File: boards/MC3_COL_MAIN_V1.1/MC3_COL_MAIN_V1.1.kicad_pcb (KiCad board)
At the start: 4 copper layers, 66 x 66 mm, 157 parts, among them J1 SUPPLY_IN, J10 MOTOR, J12 CAN, J13 HARNESS_FFC_6P, J2 SWD, J3 ENC_leaf1, J4 ENC_leaf2, J5 ENC_leaf3, J6 ENC_leaf4, J7 MOTOR, J8 MOTOR, J9 MOTOR, Q1 AO4421, SW1 SKRKAEE020, U1 AMS1117-3.3, U10 GP1S094HCZ0F, U11 GP1S094HCZ0F, U12 LM61460AANRJRR, U2 STM32U595RJT6, U3 DRV8214RTER, U4 DRV8214RTER, U5 DRV8214RTER, U6 DRV8214RTER, U7 DRV8214RTER, U8 TJA1051T/3, U9 AEDR-8300-1Q0, Y1 8MHz

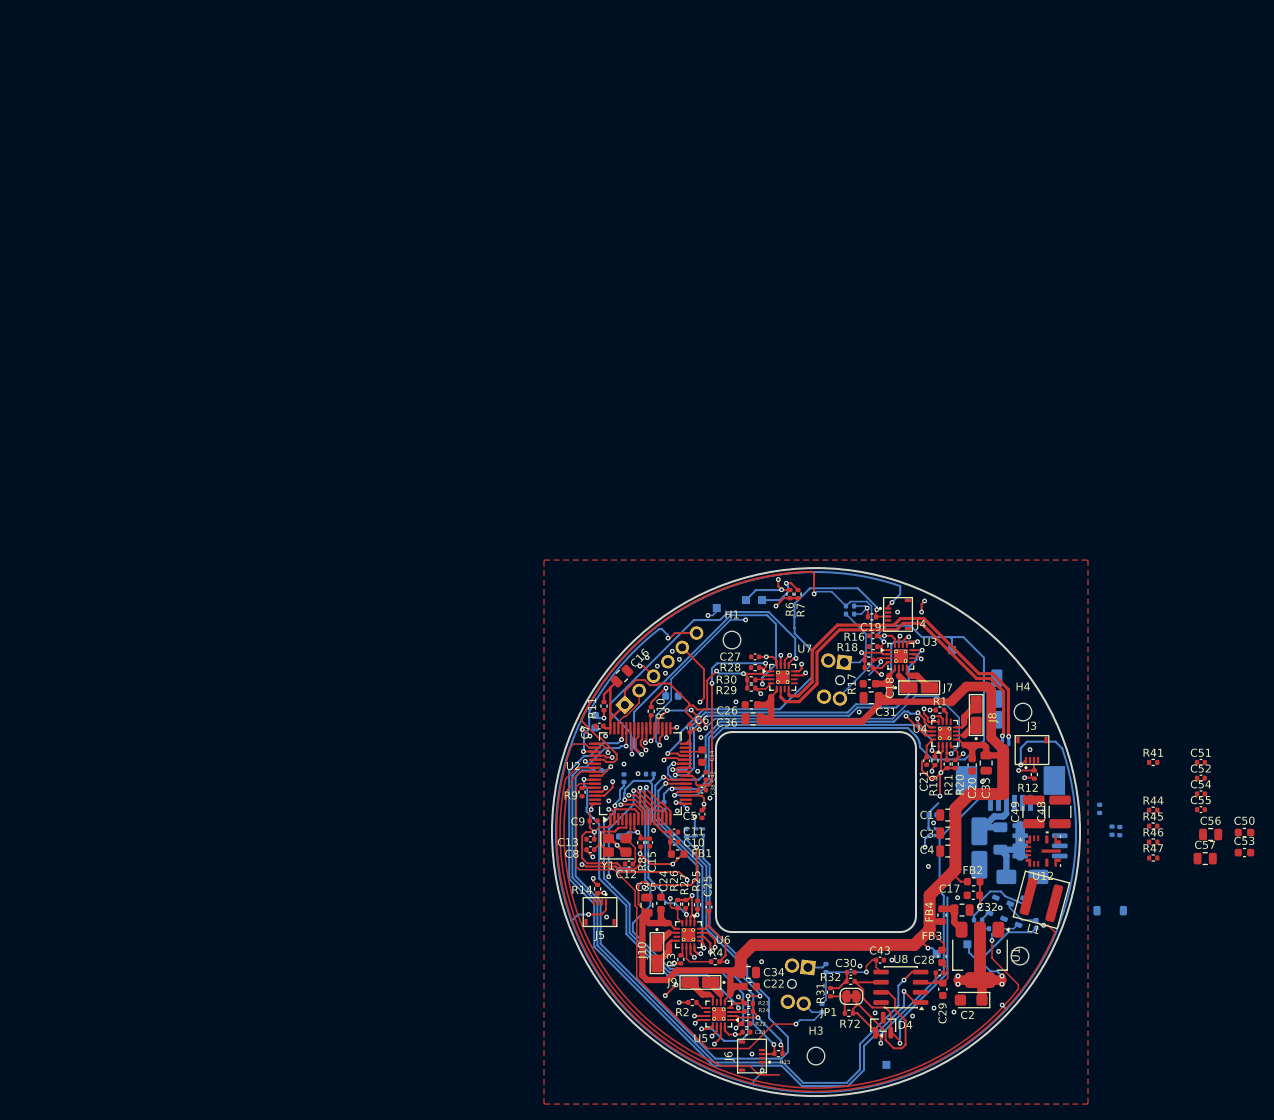
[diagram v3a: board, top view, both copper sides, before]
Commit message: V1.1: encoder FFC pin 4 -> RC_OUT_leafN (optical-fallback B channel over the open-drain ripple net); ERC 0 errors
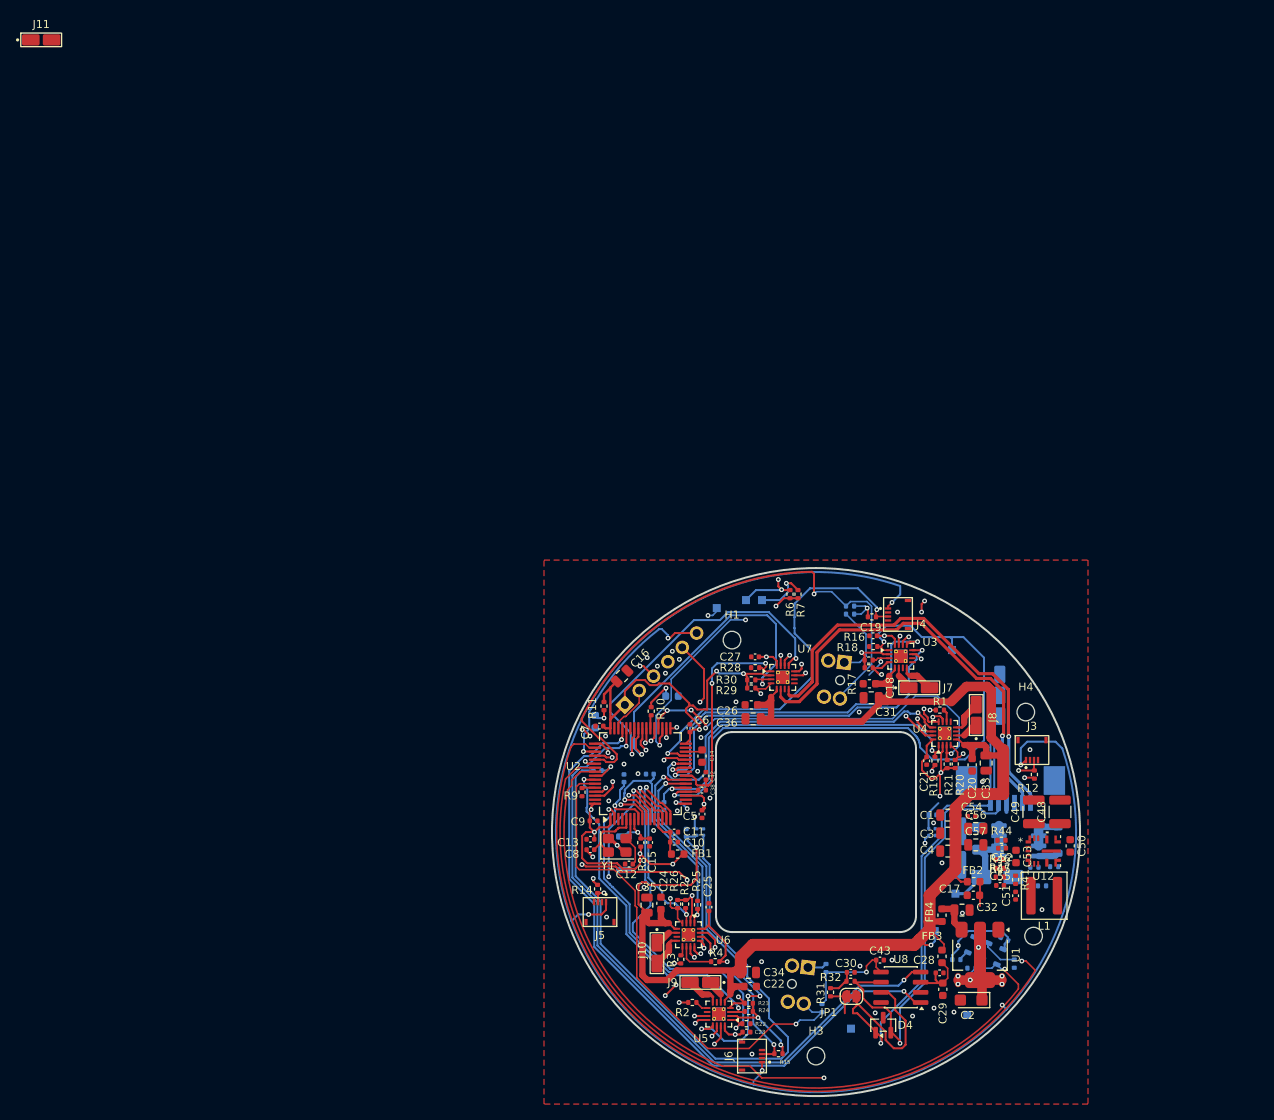
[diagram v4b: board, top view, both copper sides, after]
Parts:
- removed R72: 0R, MC3_COL_MAIN:R_0402_1005Metric
- added J11: MOTOR, MC3_COL_MAIN:SolderPads_2x_2.2x1.4mm_P2.6mm, F.Cu at (3.15, 0.97)
- moved C56 29.4 mm to (120.0, 99.5)
- moved C54 28.8 mm to (119.4, 98.0)
- moved C57 28.7 mm to (120.0, 101.6)
- moved C53 28.6 mm to (125.0, 103.0), turned to -90 degrees
- moved C51 28.5 mm to (125.0, 108.0), turned to 90 degrees
- moved C55 26.8 mm to (123.0, 106.7)
- moved C52 26.4 mm to (123.3, 102.0), turned to 180 degrees
- moved R41 22.6 mm to (125.0, 106.0), turned to -90 degrees
- moved C50 21.8 mm to (131.8, 101.7), turned to -90 degrees
- moved R45 19.6 mm to (123.0, 103.5), turned to 180 degrees
- moved R46 19.4 mm to (123.0, 104.5)
- moved R44 19.3 mm to (123.2, 101.0)
- moved R47 19.3 mm to (123.0, 105.6)
- moved R42 11.9 mm to (128.2, 106.7), turned to 0 degrees
- moved D7 11.0 mm to (130.2, 101.0), turned to -90 degrees
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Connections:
- net /Power/BUCK_RBOOT renamed Net-(U12-RBOOT)
- C51 pad 1: BUCK_SYNC -> /Power/BUCK_EN
- C51 pad 2: /Power/BUCK_EN -> BUCK_SYNC
- C55 pad 2: /Power/BUCK_FF -> Net-(C55-Pad2)
- J12 pad 1: CANH -> CANL
- J12 pad 2: CANL -> CANH
- J13 pad 1: YAW_OUT1 -> CANH
- J13 pad 2: YAW_OUT2 -> CANL
- J13 pad 5: CANH -> YAW_OUT1
- J13 pad 6: CANL -> YAW_OUT2
- R47 pad 1: /Power/BUCK_FF -> /Power/BUCK_FB
- R47 pad 2: /Power/BUCK_FB -> Net-(C55-Pad2)
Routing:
- net CANH: track 38.1 -> 79.1 mm, vias 0 -> 1
- net BUCK_SYNC: track 12.2 -> 51.6 mm, vias 0 -> 1
- net CANL: track 35.9 -> 66.7 mm
- net /CAN/CANH: track 26.5 -> 0.00 mm, vias 1 -> 0
- net +3V3: track 228.3 -> 208.4 mm
- net YAW_OUT1: track 45.4 -> 54.7 mm
- net YAW_OUT2: track 45.2 -> 53.6 mm
- net CAN1_RX: track 89.6 -> 84.2 mm
- net /Power/VIN_SW: track 0.00 -> 5.01 mm
- net CAN1_TX: track 89.3 -> 84.3 mm
- net VIN_PAD: track 8.45 -> 3.97 mm
- net VIN_PROT: track 10.2 -> 14.5 mm
- net /MCU/YAW_ENC_B: track 16.2 -> 13.2 mm, vias 1 -> 2
- net /Power/Q1_G: track 0.00 -> 2.54 mm
- net /MCU/YAW_ENC_A: track 10.9 -> 10.0 mm
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
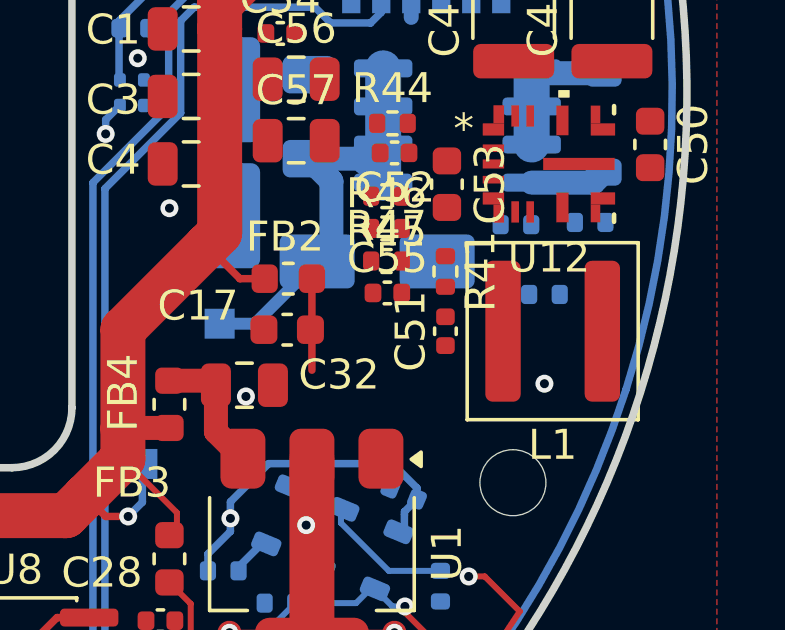
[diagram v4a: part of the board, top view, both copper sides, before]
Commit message: V1.1: encoder connector nets swapped to match placement (J3=leaf2, J4=leaf1, J5=leaf4, J6=leaf3)
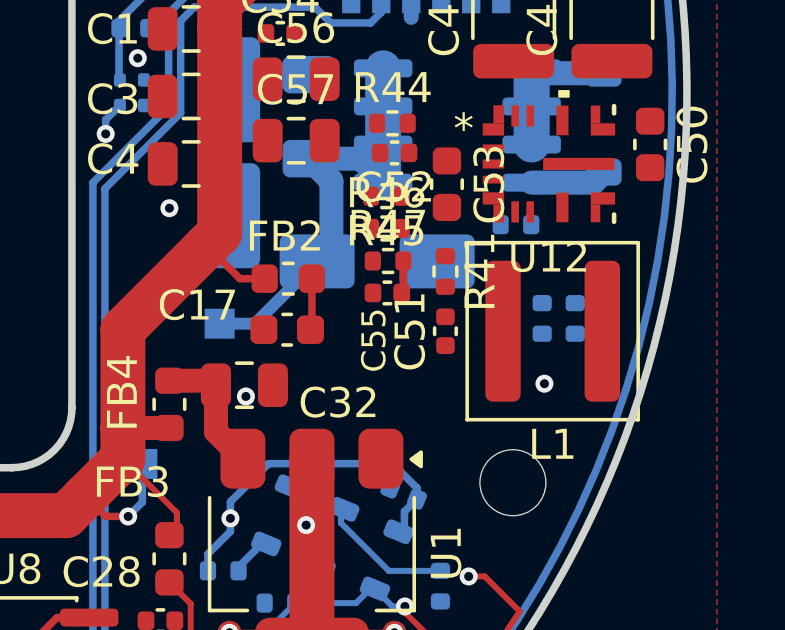
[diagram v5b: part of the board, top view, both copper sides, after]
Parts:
- moved R43 3.58 mm to (128.2, 107.5), turned to 90 degrees
- moved R42 1.30 mm to (129.3, 107.5), turned to -90 degrees
- moved R47 0.06 mm to (123.0, 105.6)
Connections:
- J3 pad 4: unconnected-(J3-Pin_4-Pad4) -> RC_OUT_leaf1
- J4 pad 4: unconnected-(J4-Pin_4-Pad4) -> RC_OUT_leaf2
- J5 pad 4: unconnected-(J5-Pin_4-Pad4) -> RC_OUT_leaf3
- J6 pad 4: unconnected-(J6-Pin_4-Pad4) -> RC_OUT_leaf4
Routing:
- net VSENS: track 51.1 -> 49.8 mm
- net Net-(C55-Pad2): track 0.00 -> 1.09 mm
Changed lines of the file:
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@@
 			(size 0.3 0.8)
 			(layers "F.Cu" "F.Mask" "F.Paste")
-			(net "unconnected-(J5-Pin_4-Pad4)")
+			(net "RC_OUT_leaf3")
 			(pinfunction "Pin_4_4")
-			(pintype "passive+no_connect")
+			(pintype "passive")
 		)
 		(pad "MP" smd rect
@@
 			(size 0.3 0.8)
 			(layers "F.Cu" "F.Mask" "F.Paste")
-			(net "unconnected-(J4-Pin_4-Pad4)")
+			(net "RC_OUT_leaf2")
 			(pinfunction "Pin_4_4")
-			(pintype "passive+no_connect")
+			(pintype "passive")
 		)
 		(pad "MP" smd rect
@@
 		(tags "capacitor")
 		(property "Reference" "C32"
-			(at 3.15 -0.35 0)
+			(at 3.15 0.6 0)
 			(layer "F.SilkS")
 			(effects
@@
 			(size 0.3 0.8)
 			(layers "F.Cu" "F.Mask" "F.Paste")
-			(net "unconnected-(J6-Pin_4-Pad4)")
+			(net "RC_OUT_leaf4")
 			(pinfunction "Pin_4_4")
-			(pintype "passive+no_connect")
+			(pintype "passive")
 		)
 		(pad "MP" smd rect
@@
 			(size 0.3 0.8)
 			(layers "F.Cu" "F.Mask" "F.Paste")
-			(net "unconnected-(J3-Pin_4-Pad4)")
+			(net "RC_OUT_leaf1")
 			(pinfunction "Pin_4_4")
-			(pintype "passive+no_connect")
+			(pintype "passive")
 		)
 		(pad "MP" smd rect
@@
 		(tags "capacitor")
 		(property "Reference" "C55"
-			(at 0 -1.16 0)
+			(at -0.44 1.575 90)
 			(layer "F.SilkS")
 			(effects
 				(font
-					(size 1 1)
+					(size 0.8 0.8)
 					(thickness 0.15)
 				)
@@
 	(footprint "MC3_COL_MAIN:R_0402_1005Metric"
 		(layer "F.Cu")
-		(at 122.985 105.61)
+		(at 123.04 105.61)
 		(descr "Resistor SMD 0402 (1005 Metric), square (rectangular) end terminal, IPC-7351 nominal, (Body size source: IPC-SM-782 page 72, https://www.pcb-3d.com/wordpress/wp-content/uploads/ipc-sm-782a_amendment_1_and_2.pdf)")
 		(tags "resistor")
@@
 		(tags "resistor")
 		(property "Reference" "R5"
-			(at 0.01 -1.25 0)
+			(at -0.025 -1.25 0)
 			(layer "B.SilkS")
 			(effects
@@
 	(footprint "MC3_COL_MAIN:R_0402_1005Metric"
 		(layer "B.Cu")
-		(at 128.25 106.725)
+		(at 129.275 107.525 -90)
 		(descr "Resistor SMD 0402 (1005 Metric), square (rectangular) end terminal, IPC-7351 nominal, (Body size source: IPC-SM-782 page 72, https://www.pcb-3d.com/wordpress/wp-content/uploads/ipc-sm-782a_amendment_1_and_2.pdf)")
 		(tags "resistor")
 		(property "Reference" "R42"
-			(at -2.716442 6.108824 0)
+			(at 0 -1.225 90)
 			(layer "B.SilkS")
 			(effects
@@
 		)
 		(property "Value" "100k"
-			(at 0 -1.17 0)
+			(at 0 -1.17 90)
 			(layer "B.Fab")
 			(effects
@@
 		)
 		(property "Datasheet" ""
-			(at 0 0 0)
+			(at 0 0 90)
 			(layer "B.Fab")
 			(hide yes)
@@
 		)
 		(property "Description" ""
-			(at 0 0 0)
+			(at 0 0 90)
 			(layer "B.Fab")
 			(hide yes)
@@
 		)
 		(property "KiLib_Generator" "SMD_2terminal_chip_molded"
-			(at 0 0 0)
+			(at 0 0 90)
 			(layer "B.SilkS")
 			(hide yes)
@@
 		(duplicate_pad_numbers_are_jumpers no)
 		(fp_line
-			(start -0.153641 -0.38)
-			(end 0.153641 -0.38)
+			(start -0.153641 0.38)
+			(end 0.153641 0.38)
 			(stroke
 				(width 0.12)
@@
 		)
 		(fp_line
-			(start -0.153641 0.38)
-			(end 0.153641 0.38)
+			(start -0.153641 -0.38)
+			(end 0.153641 -0.38)
 			(stroke
 				(width 0.12)
@@
 		)
 		(fp_text user "${REFERENCE}"
-			(at 0 0 0)
+			(at 0 0 90)
 			(layer "B.Fab")
 			(effects
@@
 		)
 		(pad "1" smd roundrect
-			(at -0.51 0)
+			(at -0.51 0 270)
 			(size 0.54 0.64)
 			(layers "B.Cu" "B.Mask" "B.Paste")
@@
 		)
 		(pad "2" smd roundrect
-			(at 0.51 0)
+			(at 0.51 0 270)
 			(size 0.54 0.64)
 			(layers "B.Cu" "B.Mask" "B.Paste")
@@
 	(footprint "MC3_COL_MAIN:R_0402_1005Metric"
 		(layer "B.Cu")
-		(at 129.775 104.325)
+		(at 128.175 107.525 90)
 		(descr "Resistor SMD 0402 (1005 Metric), square (rectangular) end terminal, IPC-7351 nominal, (Body size source: IPC-SM-782 page 72, https://www.pcb-3d.com/wordpress/wp-content/uploads/ipc-sm-782a_amendment_1_and_2.pdf)")
 		(tags "resistor")
 		(property "Reference" "R43"
-			(at 0 1.17 0)
+			(at 0 -1.25 90)
 			(layer "B.SilkS")
 			(effects
@@
 		)
 		(property "Value" "8.66k"
-			(at 0 -1.17 0)
+			(at 0 -1.17 90)
 			(layer "B.Fab")
 			(effects
@@
 		)
 		(property "Datasheet" ""
-			(at 0 0 0)
+			(at 0 0 90)
 			(layer "B.Fab")
 			(hide yes)
@@
 		)
 		(property "Description" ""
-			(at 0 0 0)
+			(at 0 0 90)
 			(layer "B.Fab")
 			(hide yes)
@@
 		)
 		(property "KiLib_Generator" "SMD_2terminal_chip_molded"
-			(at 0 0 0)
+			(at 0 0 90)
 			(layer "B.SilkS")
 			(hide yes)
@@
 		)
 		(fp_text user "${REFERENCE}"
-			(at 0 0 0)
+			(at 0 0 90)
 			(layer "B.Fab")
 			(effects
@@
 		)
 		(pad "1" smd roundrect
-			(at -0.51 0)
+			(at -0.51 0 90)
 			(size 0.54 0.64)
 			(layers "B.Cu" "B.Mask" "B.Paste")
@@
 		)
 		(pad "2" smd roundrect
-			(at 0.51 0)
+			(at 0.51 0 90)
 			(size 0.54 0.64)
 			(layers "B.Cu" "B.Mask" "B.Paste")
@@
 	)
 	(segment
-		(start 120.5 109.25)
-		(end 120.5 107.95)
-		(width 0.25)
-		(layer "F.Cu")
-		(net "VSENS")
-	)
-	(segment
 		(start 125.6 91.6)
 		(end 125.65 91.6)
@@
 	)
 	(segment
-		(start 103.6 120.71)
-		(end 103.6 122.65)
-		(width 0.25)
-		(layer "F.Cu")
-		(net "/CAN/TERM_H")
-	)
-	(segment
-		(start 101.815 120.535)
-		(end 103.775 120.535)
-		(width 0.25)
-		(layer "F.Cu")
-		(net "/CAN/TERM_H")
-	)
-	(segment
-		(start 103.775 120.535)
-		(end 103.6 120.71)
-		(width 0.25)
-		(layer "F.Cu")
-		(net "/CAN/TERM_H")
-	)
-	(segment
 		(start 91.778022 129.278022)
 		(end 88.379002 129.278022)
@@
 	)
 	(segment
+		(start 103.6 120.71)
+		(end 103.6 122.65)
+		(width 0.25)
+		(layer "F.Cu")
+		(net "/CAN/TERM_H")
+	)
+	(segment
+		(start 101.815 120.535)
+		(end 103.775 120.535)
+		(width 0.25)
+		(layer "F.Cu")
+		(net "/CAN/TERM_H")
+	)
+	(segment
+		(start 103.775 120.535)
+		(end 103.6 120.71)
+		(width 0.25)
+		(layer "F.Cu")
+		(net "/CAN/TERM_H")
+	)
+	(segment
 		(start 103.68 118.785)
 		(end 103.57 118.785)
@@
 	)
 	(segment
+		(start 123.55 105.61)
+		(end 123.55 106.62)
+		(width 0.25)
+		(layer "F.Cu")
+		(net "Net-(C55-Pad2)")
+	)
+	(segment
+		(start 123.55 106.62)
+		(end 123.495 106.675)
+		(width 0.25)
+		(layer "F.Cu")
+		(net "Net-(C55-Pad2)")
+	)
+	(segment

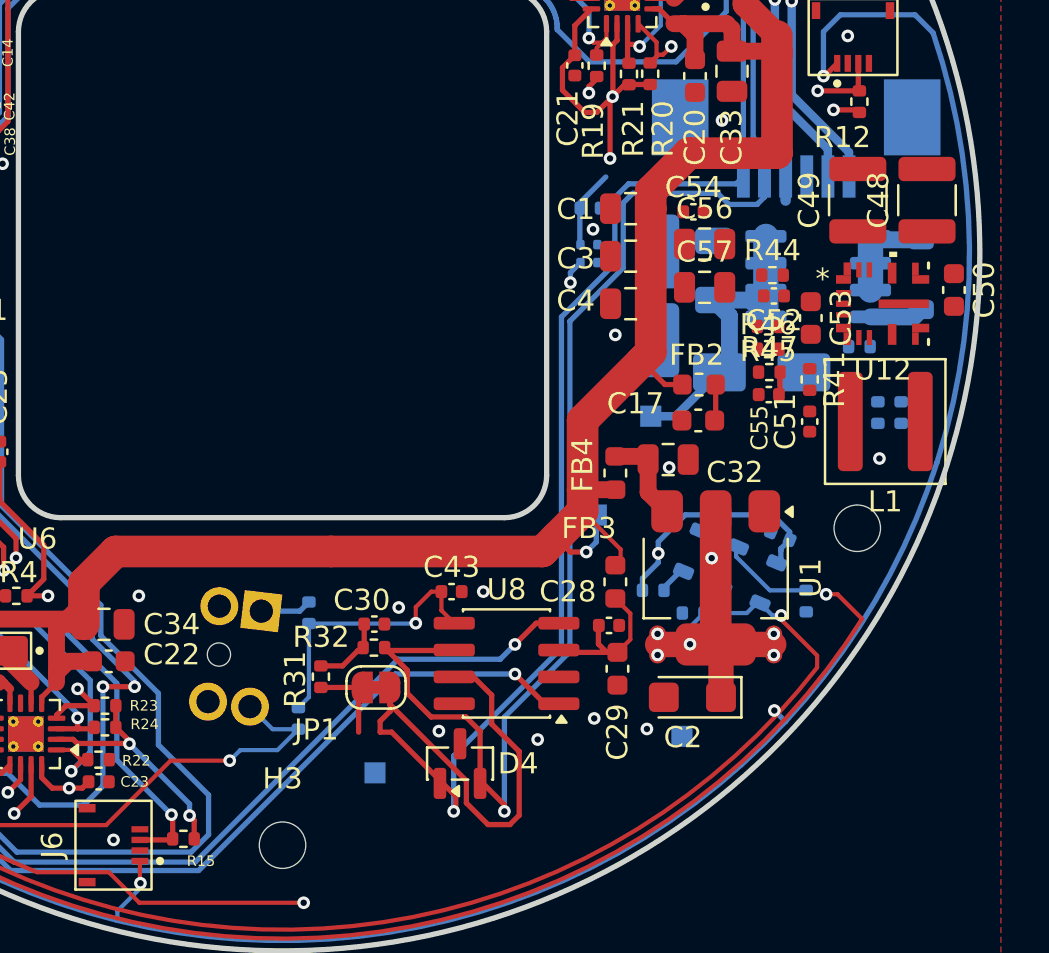
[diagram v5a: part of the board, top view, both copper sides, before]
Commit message: V1.1: ENC rename carried to MCU labels (pure rename over existing copper); pinout + firmware pages updated
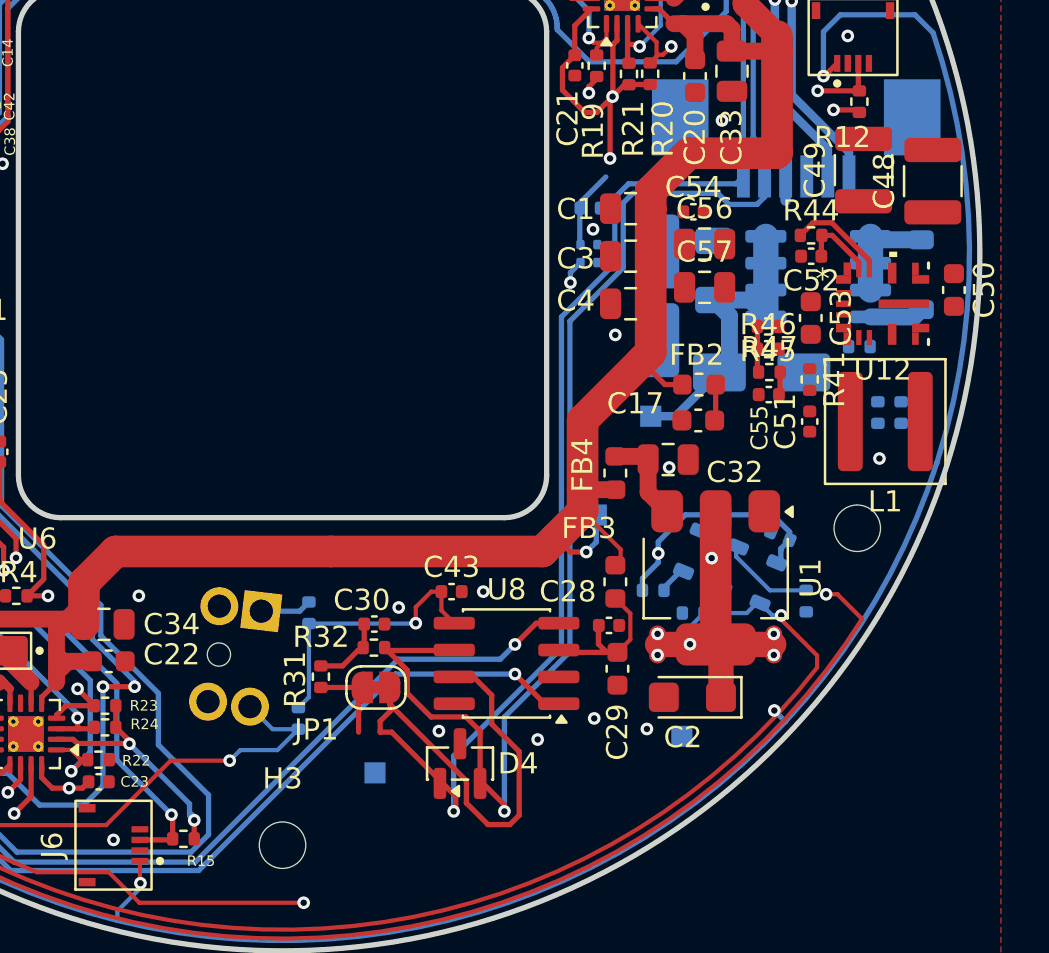
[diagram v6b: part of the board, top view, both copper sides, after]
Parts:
- moved R44 2.62 mm to (125.0, 99.1)
- moved C52 2.58 mm to (125.0, 100.1)
- moved C49 1.45 mm to (127.5, 96.0)
- moved C48 0.94 mm to (130.8, 96.6)
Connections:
- J3 pad 3: ENC_leaf1 -> ENC_leaf2
- J3 pad 4: RC_OUT_leaf1 -> RC_OUT_leaf2
- J4 pad 3: ENC_leaf2 -> ENC_leaf1
- J4 pad 4: RC_OUT_leaf2 -> RC_OUT_leaf1
- J5 pad 3: ENC_leaf3 -> ENC_leaf4
- J5 pad 4: RC_OUT_leaf3 -> RC_OUT_leaf4
- J6 pad 3: ENC_leaf4 -> ENC_leaf3
- J6 pad 4: RC_OUT_leaf4 -> RC_OUT_leaf3
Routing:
- net Net-(U12-RBOOT): track 0.00 -> 4.70 mm
- net /Power/BUCK_BOOT: track 0.00 -> 3.64 mm
- net /Power/BUCK_FB: track 0.00 -> 2.18 mm
